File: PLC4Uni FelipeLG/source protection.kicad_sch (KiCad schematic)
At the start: 9 parts

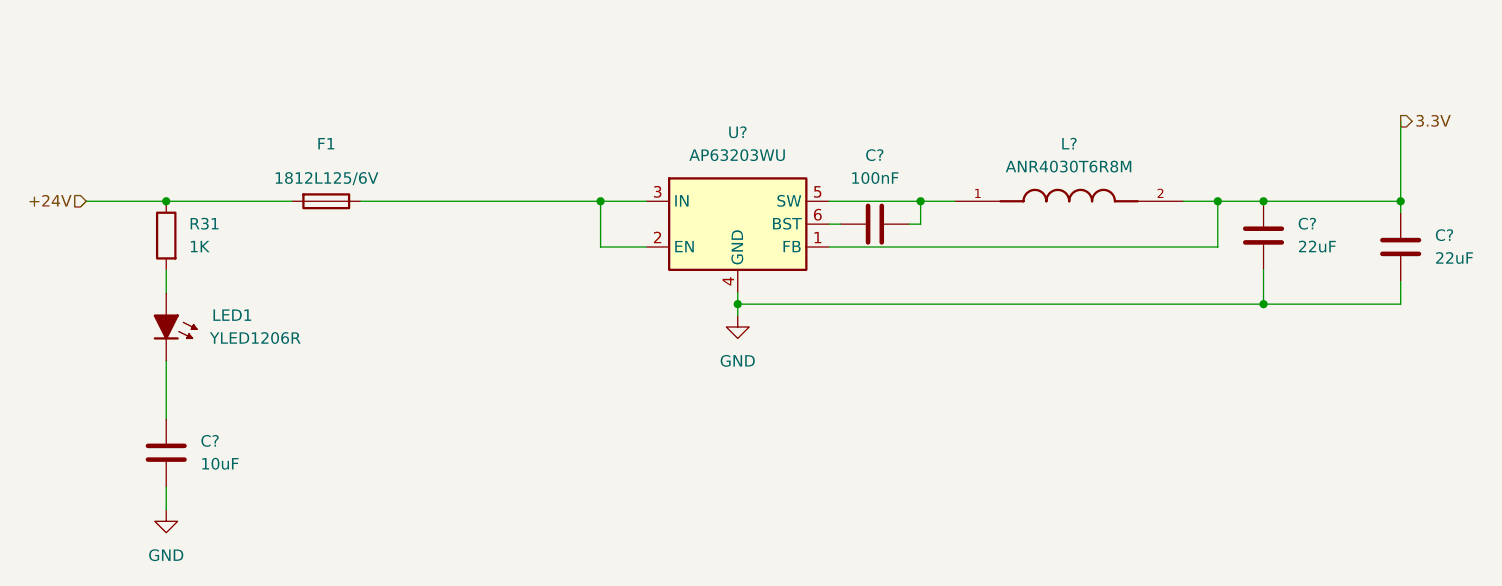
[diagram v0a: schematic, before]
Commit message: Add files via upload
Updated Circuitos corregidos y pistas agregadas
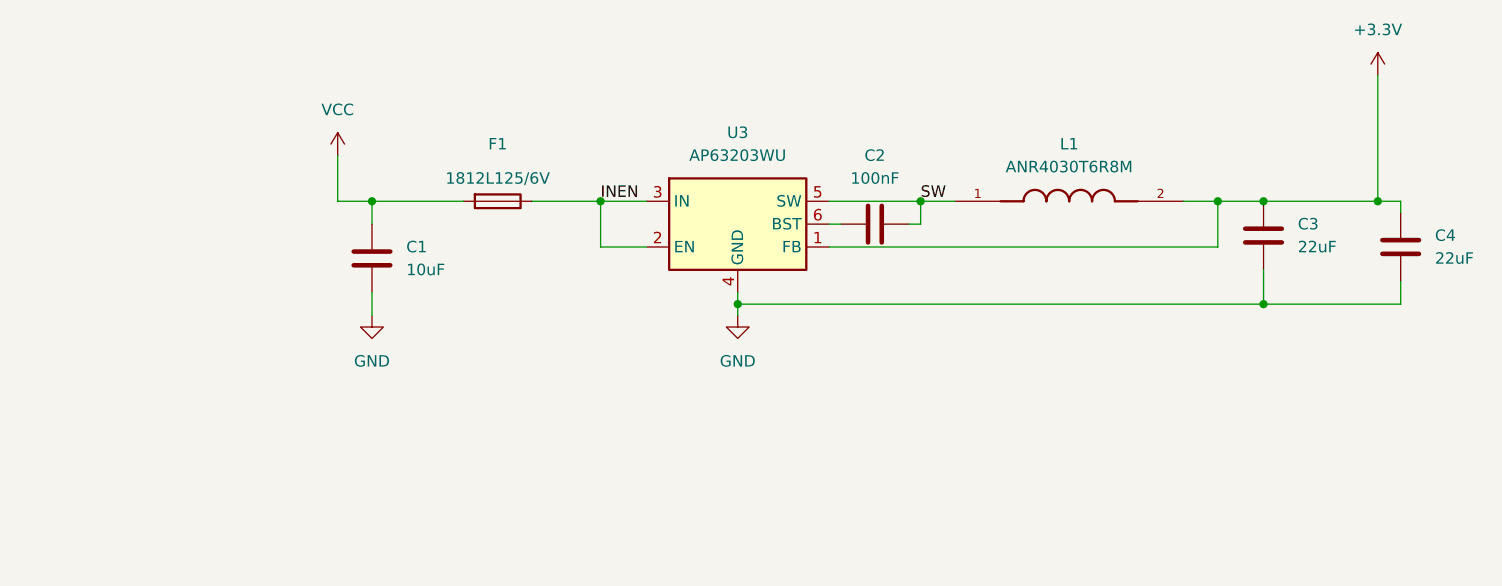
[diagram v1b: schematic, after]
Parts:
- removed LED1: LED_1.8mm_SMD, LED_SMD_AKL:LED_1.8mm_GullWing, symbol LED_AKL:LED_1.8mm_SMD
- removed R31: 1K, Resistor_SMD_AKL:R_0603_1608Metric, symbol Resistor_AKL:R_0603
- C1: renamed from C?; footprint PCM_Capacitor_SMD_AKL:C_1206_3216Metric -> Capacitor_SMD_AKL:C_0603_1608Metric
- C2: renamed from C?; footprint PCM_Capacitor_SMD_AKL:C_0805_2012Metric -> Capacitor_SMD_AKL:C_0603_1608Metric
- C3, C4: renamed from C?; footprint PCM_Capacitor_SMD_AKL:C_1206_3216Metric -> Capacitor_SMD_AKL:C_1206_3216Metric
- gave numbers to parts that had none: 2
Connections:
- net +24V is gone; now on net VCC: F1.2
- net INEN: now reaches F1.1, U3.2 (EN), U3.3 (IN)
- net SW: now reaches C2.2, L1.1, U3.5 (SW)
- net VCC: now reaches C1.1
- net 3.3V renamed +3.3V
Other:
- moved on the sheet: C1, F1
